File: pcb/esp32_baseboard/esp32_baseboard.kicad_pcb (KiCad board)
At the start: 2 copper layers, 100 x 100 mm, 60 parts, among them J1 24V_IN, J14 BUP_U, J15 FIBER, Q1 S8050, Q2 S8050, U1 WROOM-32, U2 MP1584EN, U3 TMC_SOCK, U44 PC817, U5 CH340C, U6 AMS1117-3.3, U7 TM1637, Y1 12MHz

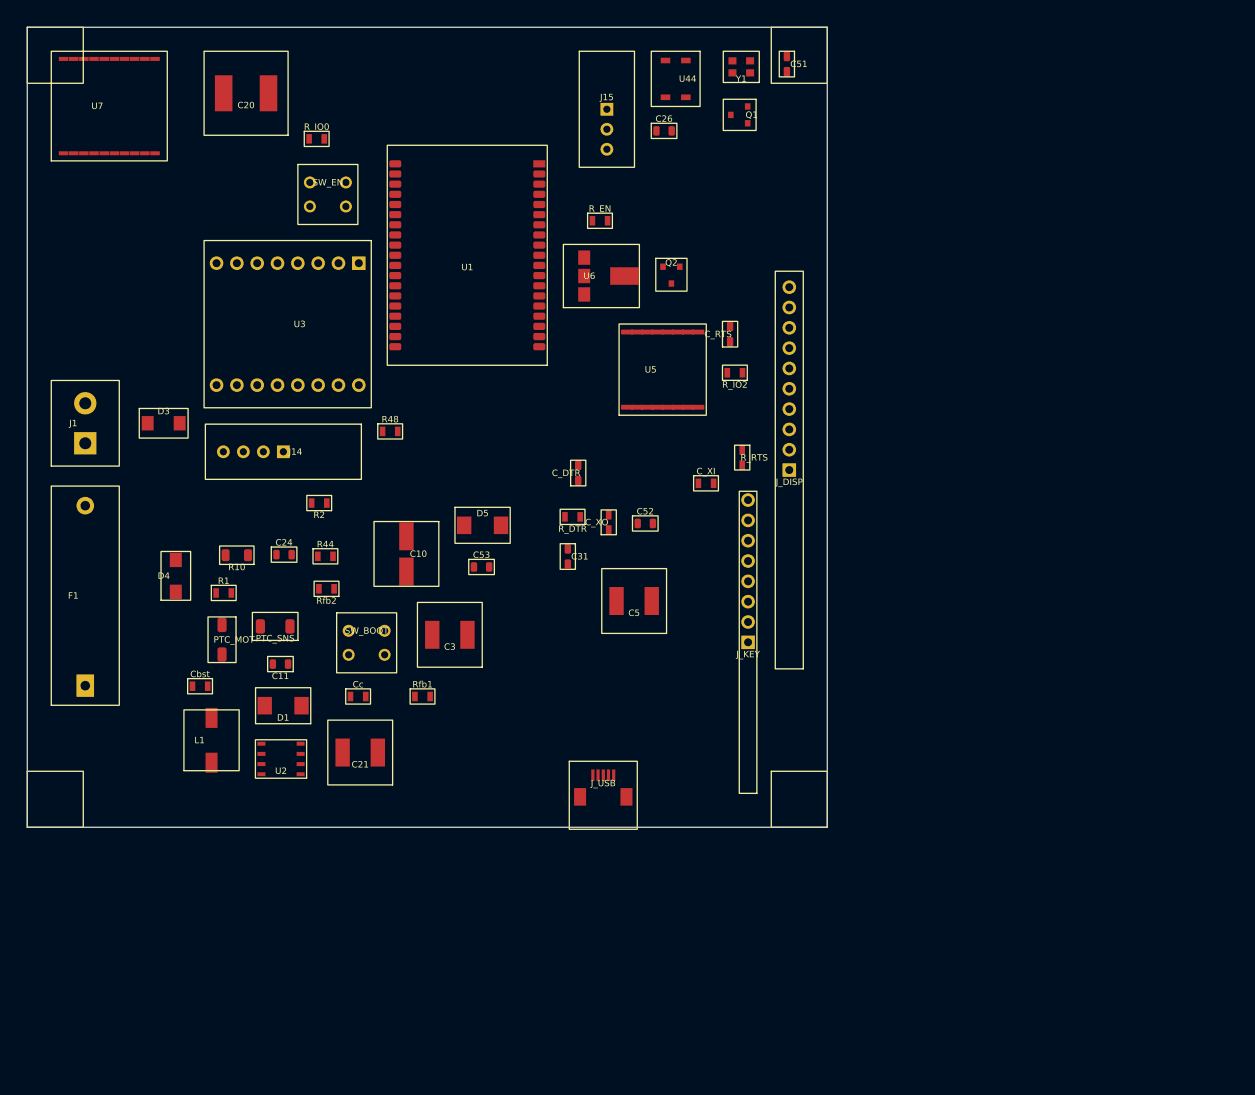
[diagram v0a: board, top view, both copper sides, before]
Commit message: thay chip esp32 bằng stm32
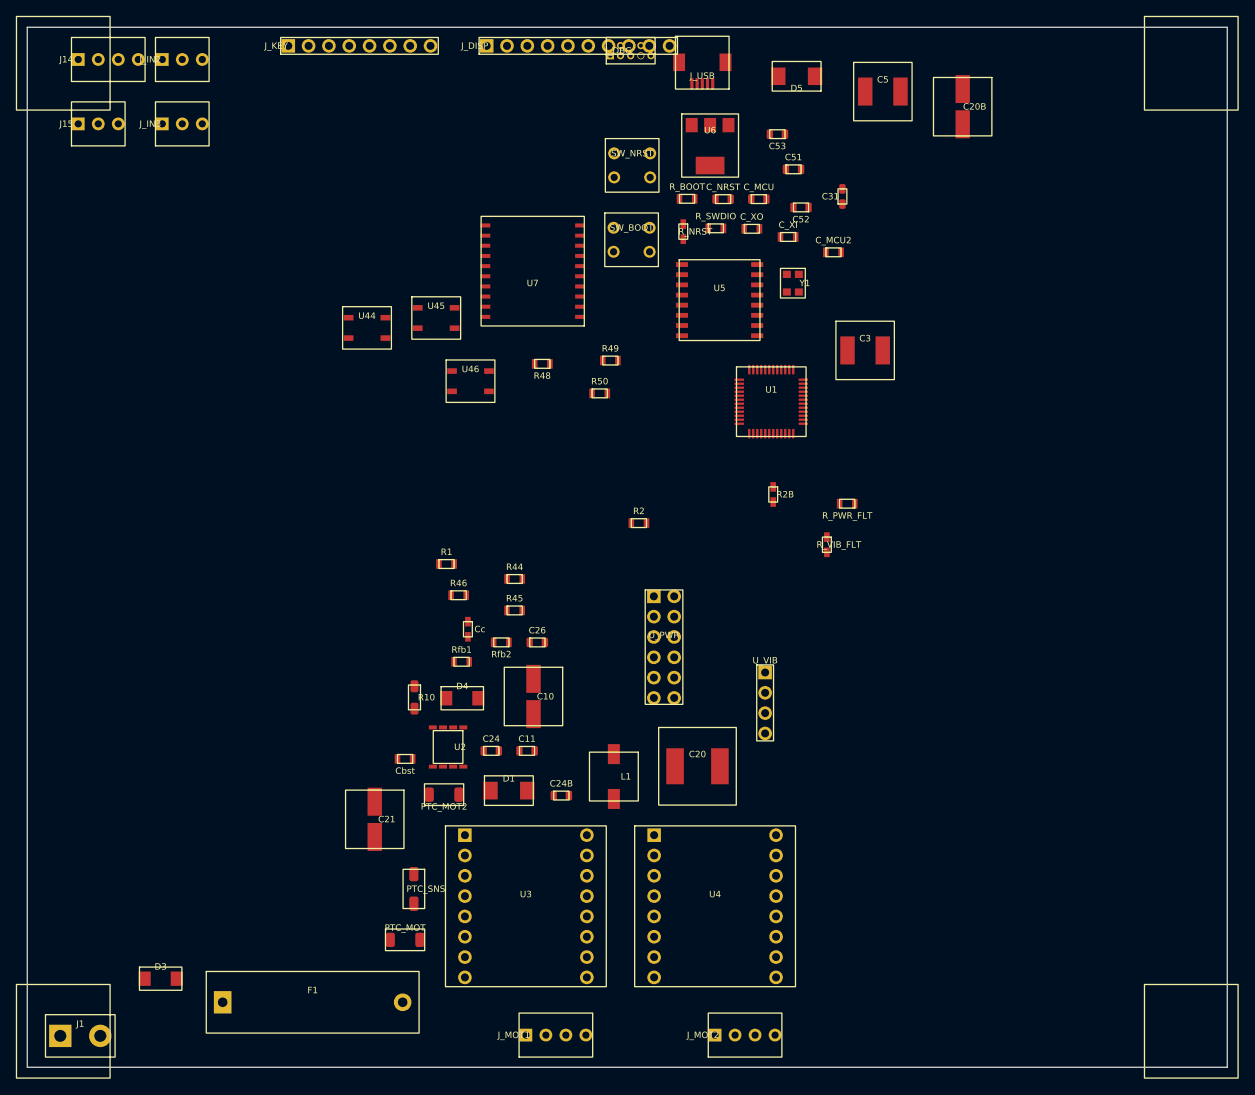
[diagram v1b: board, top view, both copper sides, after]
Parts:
- removed C_DTR, C_RTS: 100n, ESP32_Carrier:C_0805_100n
- removed Q1, Q2: S8050, ESP32_Carrier:S8050_SOT23
- removed R_DTR, R_EN, R_IO0, R_IO2, R_RTS: 10k, ESP32_Carrier:R_0805_10k
- removed SW_EN: EN, ESP32_Carrier:SW_Push_6mm
- added C20B: 220u/50V, ESP32_Carrier:CP_SMD_D6.3x5.8, F.Cu at (166.9, 59.9)
- added C24B: 100n, ESP32_Carrier:C_0805_100n, F.Cu at (116.8, 146.0)
- added C_MCU: 100n, ESP32_Carrier:C_0805_100n, F.Cu at (141.4, 71.5)
- added C_MCU2: 1u, ESP32_Carrier:C_0805, F.Cu at (150.8, 78.1)
- added C_NRST: 100n, ESP32_Carrier:C_0805_100n, F.Cu at (137.0, 71.5)
- added J_DBG: CortexDbg, ESP32_Carrier:Cortex_Debug_10, F.Cu at (125.4, 52.9)
- added J_IN2: IN2, ESP32_Carrier:JST_XH_03_Socket, F.Cu at (66.9, 54.0)
- added J_IN3: IN3, ESP32_Carrier:JST_XH_03_Socket, F.Cu at (66.9, 62.1)
- added J_MOT1: MOT1, ESP32_Carrier:Mot_XH_04_Socket, F.Cu at (112.3, 176.0)
- added J_MOT2: MOT2, ESP32_Carrier:Mot_XH_04_Socket, F.Cu at (136.0, 176.0)
- added PTC_MOT2: 1.1A, ESP32_Carrier:PTC_1812, F.Cu at (102.1, 145.9)
- added R2B: 10k, ESP32_Carrier:R_0805_10k, F.Cu at (143.2, 108.4)
- added R45: 2k2, ESP32_Carrier:R_0805_2k2, F.Cu at (110.9, 122.9)
- added R46: 2k2, ESP32_Carrier:R_0805_2k2, F.Cu at (103.9, 121.0)
- added R49: 10k, ESP32_Carrier:R_0805_10k, F.Cu at (122.9, 91.7)
- added R50: 10k, ESP32_Carrier:R_0805_10k, F.Cu at (121.6, 95.8)
- added R_BOOT: 10k, ESP32_Carrier:R_0805_10k, F.Cu at (132.5, 71.4)
- added R_NRST: 10k, ESP32_Carrier:R_0805_10k, F.Cu at (132.0, 75.5)
- added R_PWR_FLT: 10k, ESP32_Carrier:R_0805_10k, F.Cu at (152.5, 109.6)
- added R_SWDIO: 10k, ESP32_Carrier:R_0805_10k, F.Cu at (136.1, 75.1)
- added R_VIB_FLT: 10k, ESP32_Carrier:R_0805_10k, F.Cu at (149.9, 114.7)
- added SW_NRST: NRST, ESP32_Carrier:SW_Push_6mm, F.Cu at (125.6, 67.3)
- added U4: TMC2, ESP32_Carrier:TMC2209_StepStick, F.Cu at (136.0, 159.9)
- added U45: PC817, ESP32_Carrier:PC817_SOP4, F.Cu at (101.1, 86.3)
- added U46: PC817, ESP32_Carrier:PC817_SOP4, F.Cu at (105.4, 94.2)
- added U_PWR: PWR_MOD, ESP32_Carrier:PowerMod_2CH_Sock, F.Cu at (129.6, 127.5)
- added U_VIB: VIB_SSR, ESP32_Carrier:VibAC_Sock, F.Cu at (142.2, 130.7)
- SW_BOOT: value BOOT -> BOOT0
- U1: value WROOM-32 -> STM32G030C8T6; footprint ESP32_Carrier:ESP32_WROOM_32 -> ESP32_Carrier:STM32G030C8T6_LQFP48
- U3: value TMC_SOCK -> TMC1
- moved C20 101.3 mm to (133.8, 142.4), turned to 0 degrees
- moved J_KEY 94.1 mm to (82.6, 52.3), turned to 90 degrees
- moved J_USB 92.3 mm to (134.4, 54.6), turned to 180 degrees
- moved U3 78.6 mm to (112.3, 159.9), turned to 0 degrees
- moved J1 76.6 mm to (56.6, 176.1), turned to 0 degrees
- moved C5 70.9 mm to (156.9, 58.0), turned to 0 degrees
- moved D3 69.4 mm to (66.7, 168.9)
- moved D5 68.5 mm to (146.2, 56.1), turned to 180 degrees
- moved J15 66.1 mm to (56.4, 62.1), turned to 90 degrees
- moved C26 65.9 mm to (113.8, 126.9)
- moved C53 65.5 mm to (143.8, 63.4), turned to 180 degrees
- moved J_DISP 65.1 mm to (107.4, 52.3), turned to 90 degrees
- moved C3 62.9 mm to (154.7, 90.4), turned to 0 degrees
- moved SW_BOOT 60.3 mm to (125.5, 76.6)
- moved F1 58.2 mm to (85.7, 171.9), turned to 0 degrees
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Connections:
- SW_BOOT pad 1: /IO0 -> /SWCLK
- SW_BOOT pad 2: /IO0 -> /SWCLK
- SW_BOOT pad 3: GND -> +3V3
- SW_BOOT pad 4: GND -> +3V3
- U1 pad 1: GND -> (no net)
- U1 pad 10: (no net) -> /NRST
- U1 pad 11: /KEY_C0 -> /STEP
- U1 pad 12: /KEY_R3 -> /DIR
- U1 pad 13: /KEY_R2 -> /EN_TMC
- U1 pad 14: /KEY_R1 -> /BUP
- U1 pad 15: GND -> /TM_CLK
- U1 pad 16: /KEY_R0 -> /TM_DIO
- U1 pad 17: (no net) -> /STEP2
- U1 pad 18: (no net) -> /DIR2
- U1 pad 19: (no net) -> /KEY_R0
- U1 pad 2: +3V3 -> (no net)
- U1 pad 20: GND -> /KEY_R1
- U1 pad 21: (no net) -> /KEY_R2
- U1 pad 22: (no net) -> /KEY_R3
- U1 pad 23: (no net) -> /KEY_C0
- U1 pad 24: /IO2 -> /KEY_C1
- U1 pad 25: /IO0 -> /KEY_C2
- U1 pad 26: /BUP -> /KEY_C3
- U1 pad 27: /STEP -> /IN2
- U1 pad 28: /DIR -> /EN_TMC2
- U1 pad 29: /KEY_C3 -> /UART_TX
- U1 pad 3: /EN -> (no net)
- U1 pad 30: /EN_TMC -> (no net)
- U1 pad 32: (no net) -> /UART_RX
- U1 pad 33: (no net) -> /PWM_OUT1
- U1 pad 34: /UART_RX -> /PWM_OUT2
- U1 pad 35: /UART_TX -> /SWDIO
- U1 pad 36: /TM_CLK -> /SWCLK
- U1 pad 37: /TM_DIO -> (no net)
- U1 pad 38: GND -> (no net)
- U1 pad 4: (no net) -> +3V3
- U1 pad 5: (no net) -> +3V3
- U1 pad 6: (no net) -> +3V3
- U1 pad 7: (no net) -> GND
- U1 pad 8: /KEY_C2 -> (no net)
- U1 pad 9: /KEY_C1 -> (no net)
- U5 pad 10: /DTR -> (no net)
- U5 pad 15: /RTS -> (no net)
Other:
- board size 100 x 100 mm -> 150 x 130 mm
- board text added: "150x130 DIN | field jacks N/S only | W/E=rail"
- board text added: "N: SNS/KEY/DISP | S: J1 MOT USB DBG | no side jacks"
- board text removed: "100x100 placement-only — ANT keepout north of U1; J1 west"
- board text removed: "ANT KEEPOUT"
- board text removed: "J_DISP=7SEG ext | J_KEY=keypad ext | J14/J15 fit ONE"
